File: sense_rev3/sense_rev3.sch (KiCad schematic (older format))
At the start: 2 parts

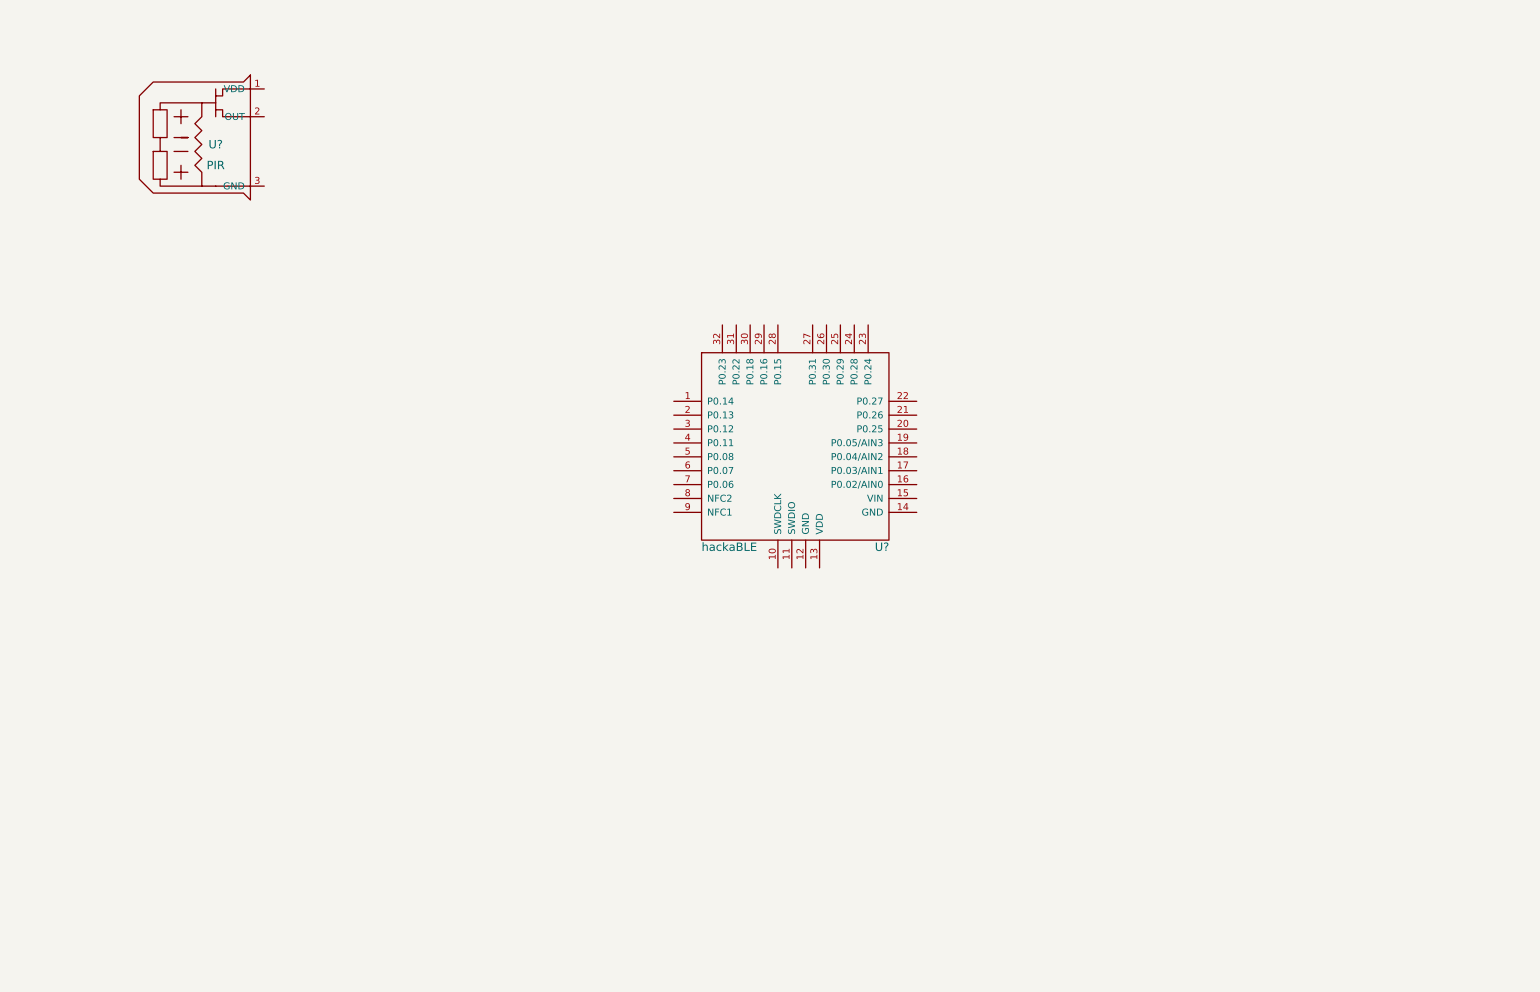
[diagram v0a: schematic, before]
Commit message: Sense rev3's schematic is done
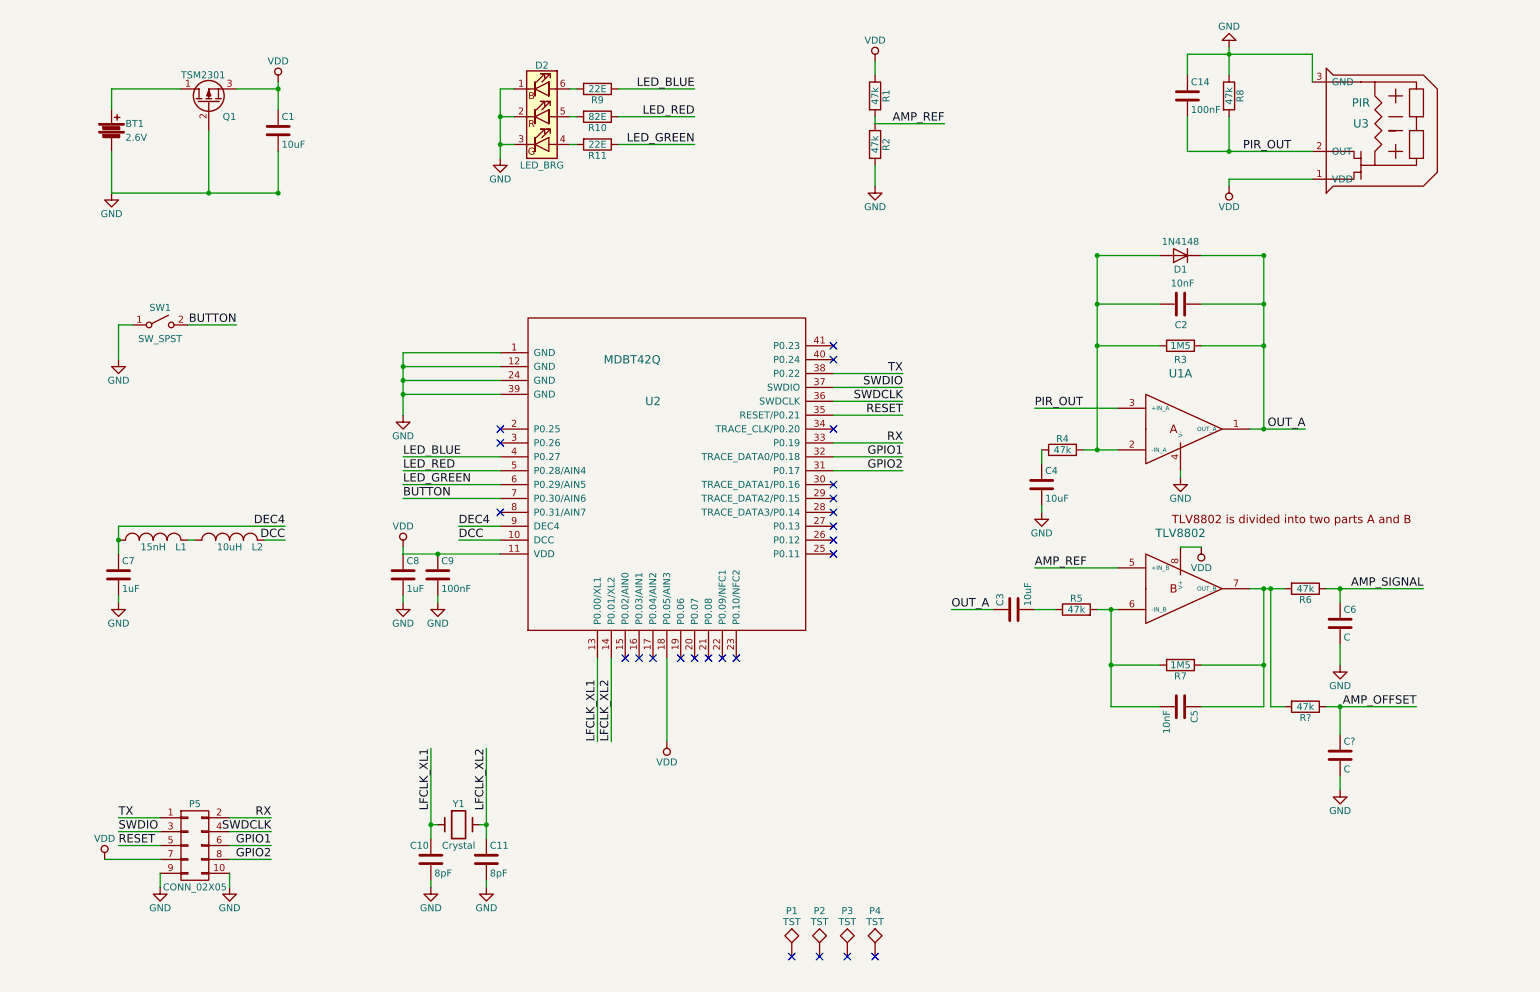
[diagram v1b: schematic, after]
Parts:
- removed U?: hackaBLE, detect_trigger:hackable_footprint, symbol hackaBLE
- added BT1: 2.6V, symbol Battery
- added C1, C3, C4: 10uF, Capacitors_SMD:C_0805, symbol C
- added C10, C11: 8pF, Capacitors_SMD:C_0805, symbol C
- added C14: 100nF, symbol C
- added C2, C5: 10nF, Capacitors_SMD:C_0805, symbol C
- added C6, C?: C, symbol C
- added C7, C8: 1uF, Capacitors_SMD:C_0805, symbol C
- added C9: 100nF, Capacitors_SMD:C_0805, symbol C
- added D1: 1N4148, symbol D
- added D2: LED_BRG, LEDs:LED_RGB_5050-6, symbol LED_BRG
- added L1: 15nH, symbol INDUCTOR_SMALL
- added L2: 10uH, symbol INDUCTOR_SMALL
- added P1, P2, P3, P4: TST, symbol TST
- added P5: CONN_02X05, symbol CONN_02X05
- added Q1: TSM2301, TO_SOT_Packages_SMD:SOT-23, symbol Q_PMOS_DGS
- added R1, R2, R4, R5, R6, R8, R?: 47k, Resistors_SMD:R_0805, symbol R
- added R10: 82E, Resistors_SMD:R_0805, symbol R
- added R11, R9: 22E, Resistors_SMD:R_0805, symbol R
- added R3, R7: 1M5, Resistors_SMD:R_0805, symbol R
- added SW1: SW_SPST, symbol SW_SPST
- added U1: TLV8802, symbol TLV8802
- added U2: MDBT42Q, symbol MDBT42Q
- added Y1: Crystal, symbol Crystal
- gave numbers to parts that had none: 1
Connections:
- net VDD: now reaches U3.1 (VDD)
- net VDD: now also C1.1, C8.1, C9.1, P5.7 (P7), Q1.3 (S), R1.1, U1.8 (V+), U2.11 (VDD), U2.18 (P0.05/AIN3)
- net PIR_OUT: now reaches U3.2 (OUT)
- net PIR_OUT: now also C14.2, R8.2, U1.3 (+IN_A)
- net GND: now reaches U3.3 (GND)
- net GND: now also BT1.2, C1.2, C10.2, C11.2, C14.1, C4.2, C6.2, C7.2, C8.2, C9.2, C?.2, D2.1 (RK), D2.2 (GK), D2.3 (BK), P5.10 (P10), P5.9 (P9), Q1.2 (G), R2.2, R8.1, SW1.1 (A), U1.4 (V-), U2.1 (GND), U2.12 (GND), U2.24 (GND), U2.39 (GND)
- new net: BT1.1, Q1.1 (D)
- new net: L1.2, L2.1
- new net: C5.1, R6.2, R7.1, R?.2, U1.7 (OUT_B)
- new net: C5.2, R5.2, R7.2, U1.6 (-IN_B)
- new net: C3.2, R5.1
- new net: C2.1, D1.2 (A), R3.1, R4.2, U1.2 (-IN_A)
- new net: C4.1, R4.1
- new net: D2.4 (BA), R11.2
- new net: D2.5 (GA), R10.2
- new net: D2.6 (RA), R9.2
- new net AMP_OFFSET: C?.1, R?.1
- new net AMP_REF: R1.2, R2.1, U1.5 (+IN_B)
- new net AMP_SIGNAL: C6.1, R6.1
- new net BUTTON: SW1.2 (B), U2.7 (P0.30/AIN6)
- new net DCC: L2.2, U2.10 (DCC)
- new net DEC4: C7.1, L1.1, U2.9 (DEC4)
- new net GPIO1: P5.6 (P6), U2.32 (TRACE_DATA0/P0.18)
- new net GPIO2: P5.8 (P8), U2.31 (P0.17)
- new net LED_BLUE: R9.1, U2.4 (P0.27)
- new net LED_GREEN: R11.1, U2.6 (P0.29/AIN5)
- new net LED_RED: R10.1, U2.5 (P0.28/AIN4)
- new net LFCLK_XL1: C10.1, U2.13 (P0.00/XL1), Y1.1
- new net LFCLK_XL2: C11.1, U2.14 (P0.01/XL2), Y1.2
- new net OUT_A: C2.2, C3.1, D1.1 (K), R3.2, U1.1 (OUT_A)
- new net RESET: P5.5 (P5), U2.35 (RESET/P0.21)
- new net RX: P5.2 (P2), U2.33 (P0.19)
- new net SWDCLK: P5.4 (P4), U2.36 (SWDCLK)
- new net SWDIO: P5.3 (P3), U2.37 (SWDIO)
- new net TX: P5.1 (P1), U2.38 (P0.22)
- no-connect marks 0 -> 24
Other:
- moved on the sheet: U3

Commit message: Sense_rev3 PCB complete
Completed the Schematics and PCB design for sense_rev3.
Created project wise footprint and schematic libraries.
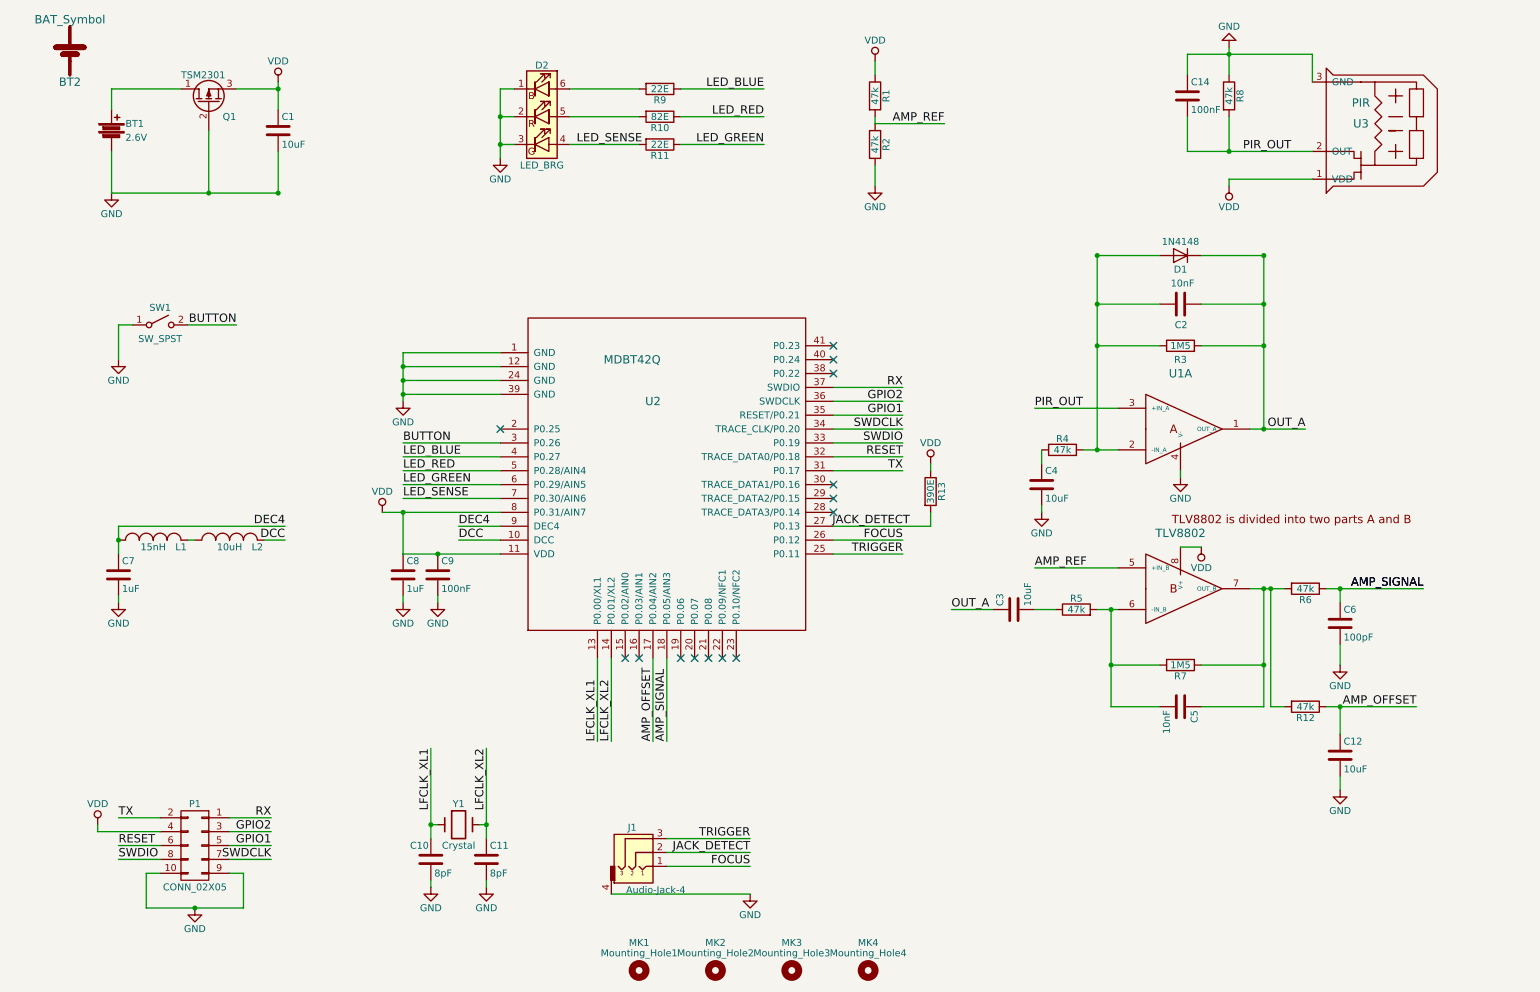
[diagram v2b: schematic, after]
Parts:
- removed P1, P2, P3, P4: TST, symbol TST
- added BT2: BAT_Symbol, sense_rev3:BT_Symbol, symbol BAT_Symbol
- added J1: Audio-Jack-4, Connectors_Molex:Molex_KK-6410-04_04x2.54mm_Straight, symbol Audio-Jack-4
- added MK1: Mounting_Hole1, Mounting_Holes:MountingHole_3.2mm_M3, symbol Mounting_Hole
- added MK2: Mounting_Hole2, Mounting_Holes:MountingHole_3.2mm_M3, symbol Mounting_Hole
- added MK3: Mounting_Hole3, Mounting_Holes:MountingHole_3.2mm_M3, symbol Mounting_Hole
- added MK4: Mounting_Hole4, Mounting_Holes:MountingHole_3.2mm_M3, symbol Mounting_Hole
- added R13: 390E, Resistors_SMD:R_0805, symbol R
- BT1, SW1: footprint (none) -> Connectors_Molex:Molex_KK-6410-02_02x2.54mm_Straight
- C12: renamed from C?; value C -> 10uF; footprint (none) -> Capacitors_SMD:C_0805
- C14: footprint (none) -> Capacitors_SMD:C_0805
- C6: value C -> 100pF; footprint (none) -> Capacitors_SMD:C_0805
- D1: footprint (none) -> Diodes_SMD:D_MiniMELF
- L1, L2: footprint (none) -> Inductors_SMD:L_0805
- P1: renamed from P5; footprint (none) -> snap_fp:prog_connect
- U1: footprint (none) -> Housings_SSOP:SSOP-8_2.95x2.8mm_Pitch0.65mm
- U2: footprint (none) -> detect_trigger:mdbt42Q
- U3: footprint (none) -> detect_trigger:PIR_TO5
- Y1: footprint (none) -> Crystals:Crystal_C38-LF_d3.0mm_l8.0mm_Horizontal
- gave numbers to parts that had none: 1
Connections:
- net AMP_OFFSET: now also U2.17 (P0.04/AIN2)
- net AMP_SIGNAL: now also U2.18 (P0.05/AIN3)
- net BUTTON: now also U2.3 (P0.26); no longer U2.7 (P0.30/AIN6)
- net GND: now also J1.4
- net GPIO1: now also P1.5 (P5), U2.35 (RESET/P0.21); no longer P1.6 (P6), U2.32 (TRACE_DATA0/P0.18)
- net GPIO2: now also P1.3 (P3), U2.36 (SWDCLK); no longer P1.8 (P8), U2.31 (P0.17)
- net RESET: now also P1.6 (P6), U2.32 (TRACE_DATA0/P0.18); no longer P1.5 (P5), U2.35 (RESET/P0.21)
- net RX: now also P1.1 (P1), U2.37 (SWDIO); no longer P1.2 (P2), U2.33 (P0.19)
- net SWDCLK: now also P1.7 (P7), U2.34 (TRACE_CLK/P0.20); no longer P1.4 (P4), U2.36 (SWDCLK)
- net SWDIO: now also P1.8 (P8), U2.33 (P0.19); no longer P1.3 (P3), U2.37 (SWDIO)
- net TX: now also P1.2 (P2), U2.31 (P0.17); no longer P1.1 (P1), U2.38 (P0.22)
- net VDD: now also P1.4 (P4), U2.8 (P0.31/AIN7), R13.1; no longer P1.7 (P7), U2.18 (P0.05/AIN3)
- net TRIGGER: now reaches U2.25 (P0.11)
- net TRIGGER: now also J1.3
- net FOCUS: now reaches U2.26 (P0.12)
- net FOCUS: now also J1.1
- net JACK_DETECT: now reaches U2.27 (P0.13)
- net JACK_DETECT: now also J1.2, R13.2
- net LED_SENSE: now reaches D2.4 (BA), R11.2
- net LED_SENSE: now also U2.7 (P0.30/AIN6)
- no-connect marks 24 -> 14
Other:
- moved on the sheet: R10, R11, R9

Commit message: Updated footprints and other files
.pretty files are updated as per the project.
Added images of completed PCBs.
Updated schematics (component names and values).
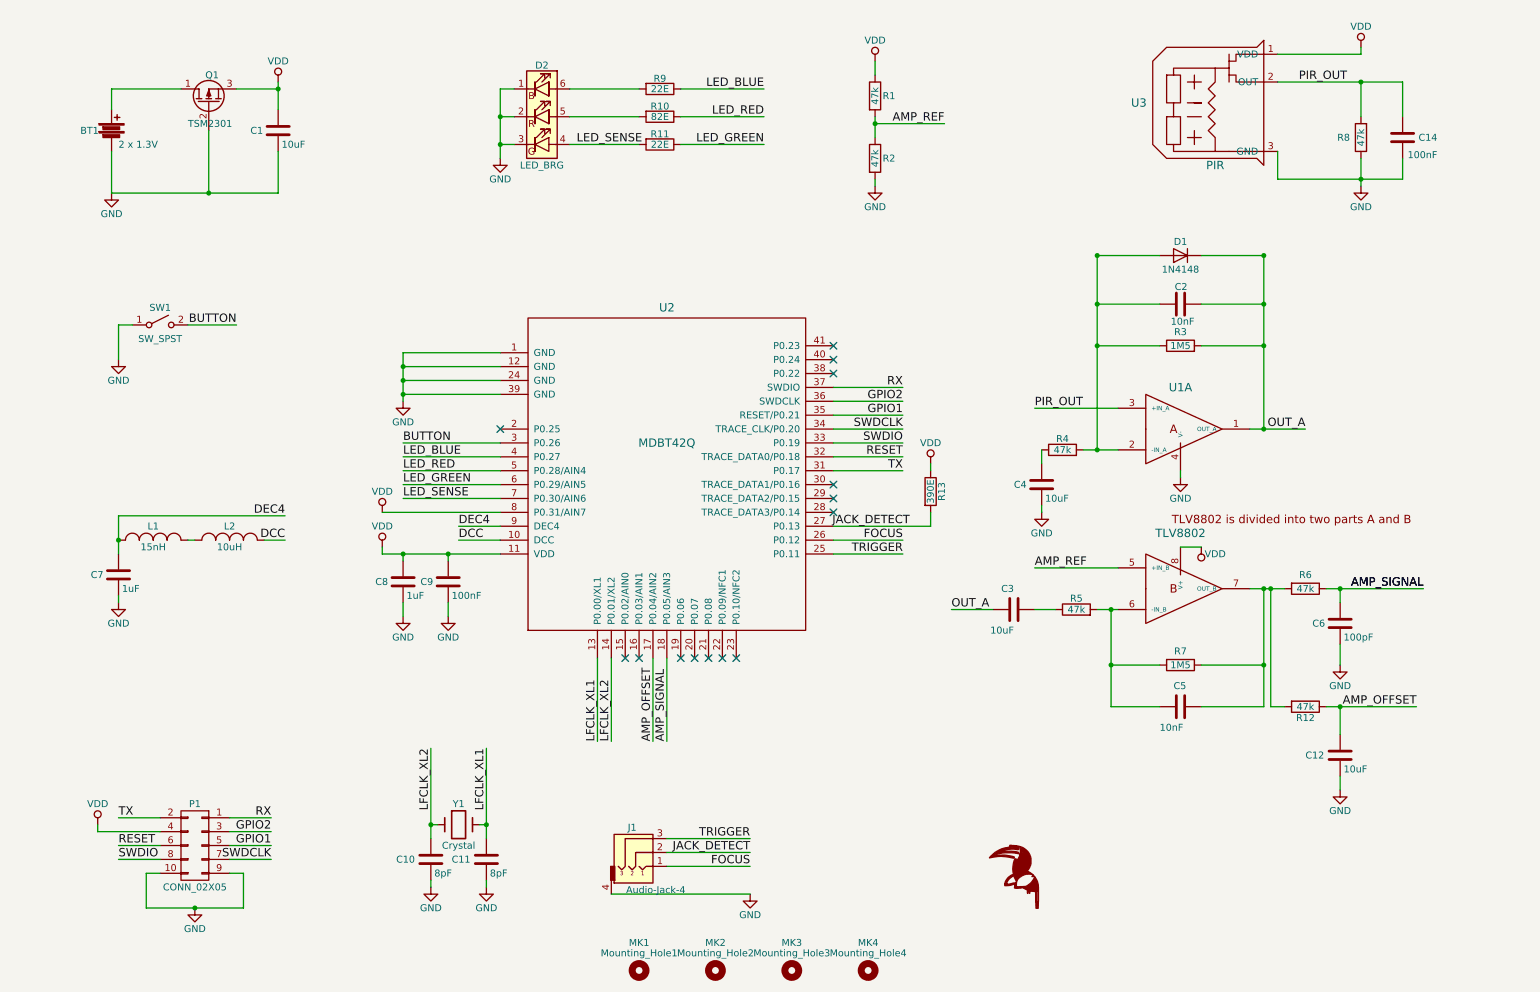
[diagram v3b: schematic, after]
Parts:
- removed BT2: BAT_Symbol, sense_rev3:BT_Symbol, symbol BAT_Symbol
- BT1: value 2.6V -> 2 x 1.3V; footprint Connectors_Molex:Molex_KK-6410-02_02x2.54mm_Straight -> sense_rev3_fp:Molex_KK-6410-02_02x2.54mm_Straight
- C1, C10, C11, C12, C14, C2, C3, C4, C5, C6, C7, C8, C9: footprint Capacitors_SMD:C_0805 -> sense_rev3_fp:C_0805
- D1: footprint Diodes_SMD:D_MiniMELF -> sense_rev3_fp:D_MiniMELF
- D2: footprint LEDs:LED_RGB_5050-6 -> sense_rev3_fp:LED_RGB_5050-6
- J1: footprint Connectors_Molex:Molex_KK-6410-04_04x2.54mm_Straight -> sense_rev3_fp:Molex_KK-6410-04_04x2.54mm_Straight
- L1, L2: footprint Inductors_SMD:L_0805 -> sense_rev3_fp:L_0805
- MK1, MK2, MK3, MK4: footprint Mounting_Holes:MountingHole_3.2mm_M3 -> sense_rev3_fp:MountingHole_3.2mm_M3
- P1: footprint snap_fp:prog_connect -> sense_rev3_fp:prog_connect
- Q1: footprint TO_SOT_Packages_SMD:SOT-23 -> sense_rev3_fp:SOT-23
- R1, R10, R11, R12, R13, R2, R3, R4, R5, R6, R7, R8, R9: footprint Resistors_SMD:R_0805 -> sense_rev3_fp:R_0805
- SW1: footprint Connectors_Molex:Molex_KK-6410-02_02x2.54mm_Straight -> sense_rev3_fp:Molex_KK-6410-02_02x2.54mm_Straight
- U1: footprint Housings_SSOP:SSOP-8_2.95x2.8mm_Pitch0.65mm -> sense_rev3_fp:SSOP-8_2.95x2.8mm_Pitch0.65mm
- U2: footprint detect_trigger:mdbt42Q -> sense_rev3_fp:mdbt42Q
- U3: footprint detect_trigger:PIR_TO5 -> sense_rev3_fp:PIR_TO5
- Y1: footprint Crystals:Crystal_C38-LF_d3.0mm_l8.0mm_Horizontal -> sense_rev3_fp:Crystal_C38-LF_d3.0mm_l8.0mm_Horizontal
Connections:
- net LFCLK_XL1: now also C11.1, Y1.2; no longer C10.1, Y1.1
- net LFCLK_XL2: now also C10.1, Y1.1; no longer C11.1, Y1.2
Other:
- moved on the sheet: C14, C8, C9, R2, R8, U3

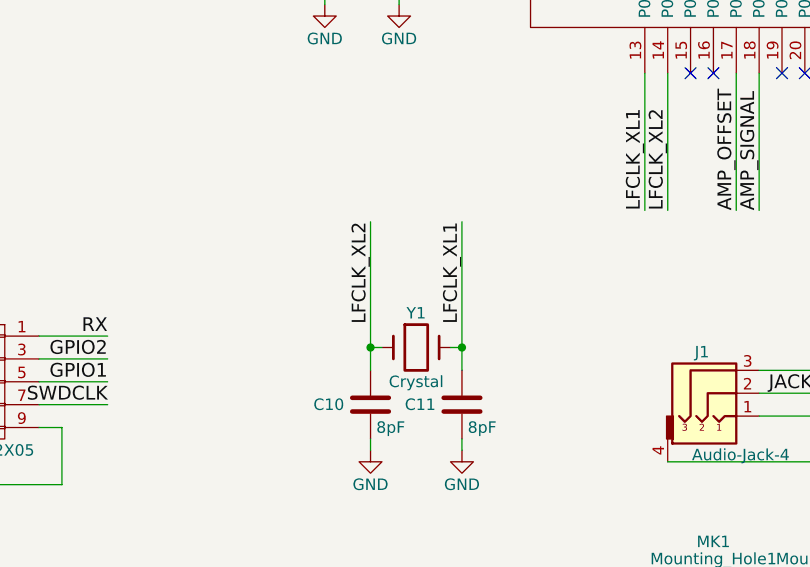
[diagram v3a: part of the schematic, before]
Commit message: Small changes in PCB
Changed the crystal orientation,
moved reference marking away from vias,
moved the track too close to PIR_OUT in bottom layer.
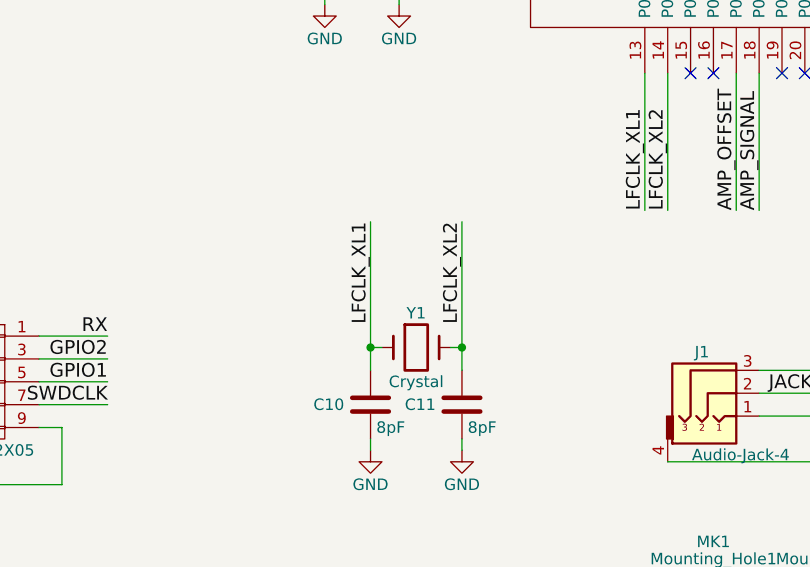
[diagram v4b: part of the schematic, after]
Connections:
- net LFCLK_XL1: now also C10.1, Y1.1; no longer C11.1, Y1.2
- net LFCLK_XL2: now also C11.1, Y1.2; no longer C10.1, Y1.1
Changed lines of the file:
@@
 	1    0    0    -1
 $EndComp
+Text Label 3500 5950 3    60   ~ 0
+LFCLK_XL1
 Text Label 3900 5950 3    60   ~ 0
-LFCLK_XL1
-Text Label 3500 5950 3    60   ~ 0
 LFCLK_XL2
 $Comp
